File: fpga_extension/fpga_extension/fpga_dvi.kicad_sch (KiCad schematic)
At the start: 5 parts

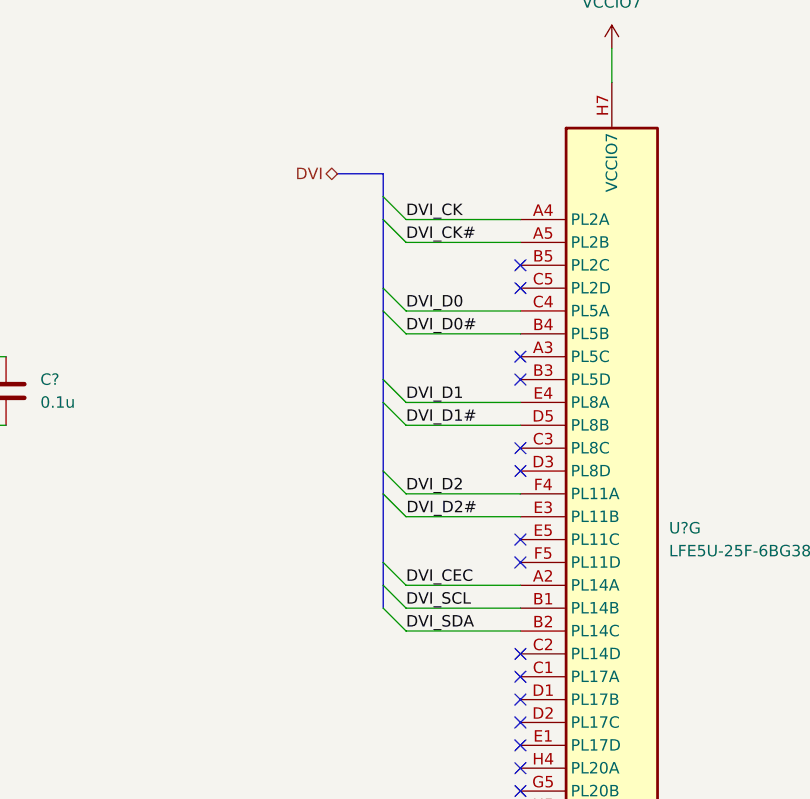
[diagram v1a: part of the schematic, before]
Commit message: gpu and motherboard passes tests, now time for fpga
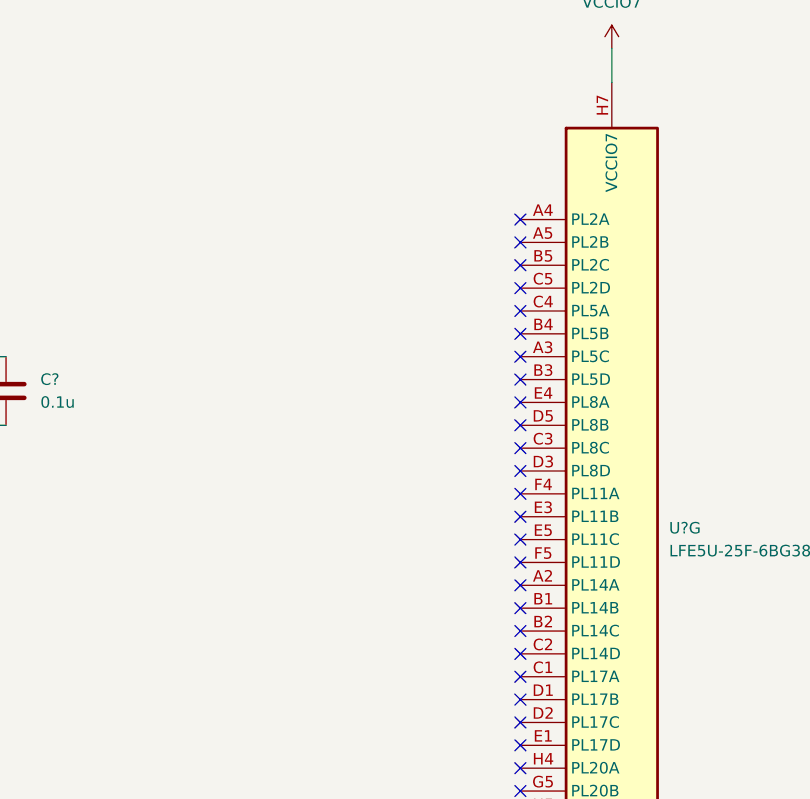
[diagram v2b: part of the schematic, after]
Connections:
- net DVI_CEC: no longer names the net of U?.A2 (PL14A)
- net DVI_CK: no longer names the net of U?.A4 (PL2A)
- net DVI_CK#: no longer names the net of U?.A5 (PL2B)
- net DVI_D0: no longer names the net of U?.C4 (PL5A)
- net DVI_D0#: no longer names the net of U?.B4 (PL5B)
- net DVI_D1: no longer names the net of U?.E4 (PL8A)
- net DVI_D1#: no longer names the net of U?.D5 (PL8B)
- net DVI_D2: no longer names the net of U?.F4 (PL11A)
- net DVI_D2#: no longer names the net of U?.E3 (PL11B)
- net DVI_SCL: no longer names the net of U?.B1 (PL14B)
- net DVI_SDA: no longer names the net of U?.B2 (PL14C)
- no-connect marks 21 -> 32

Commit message: refactored mainboard schematic
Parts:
- removed C?: 10u, Capacitor_SMD:C_0603_1608Metric_Pad1.08x0.95mm_HandSolder, symbol Device:C
- removed C? (x3): 0.1u, Capacitor_SMD:C_0201_0603Metric_Pad0.64x0.40mm_HandSolder, symbol Device:C
- removed U?: LFE5U-25F-6BG381x, Package_BGA:Lattice_caBGA-381_17.0x17.0mm_Layout20x20_P0.8mm_Ball0.4mm_Pad0.4mm_NSMD, symbol fpga_extension_library:LFE5U-25F-6BG381x
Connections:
- no-connect marks 32 -> 0
